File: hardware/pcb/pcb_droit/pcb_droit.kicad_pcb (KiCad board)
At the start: 2 copper layers, 31 x 60 mm, 19 parts, among them P1 TE-FFC-10-0.5

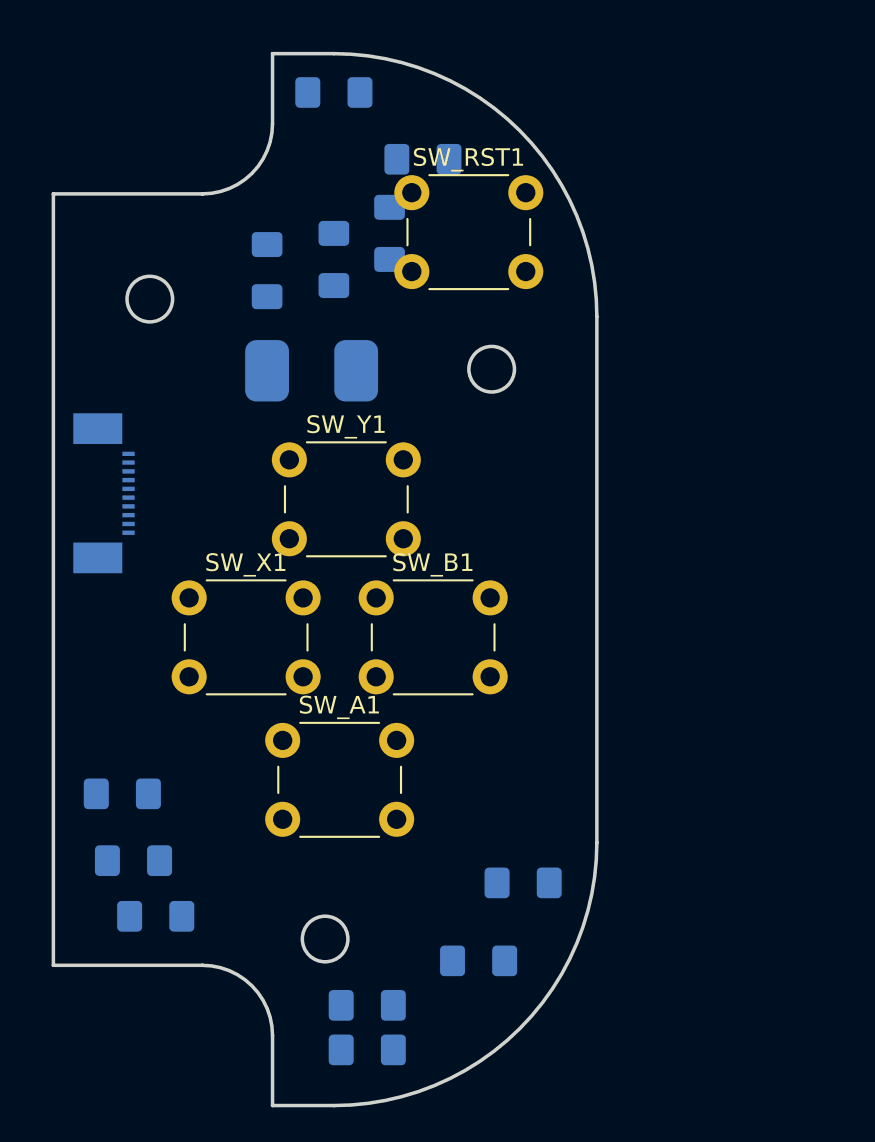
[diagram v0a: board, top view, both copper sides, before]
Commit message: Modifications des fonts et debut de la creation du drivers de touches
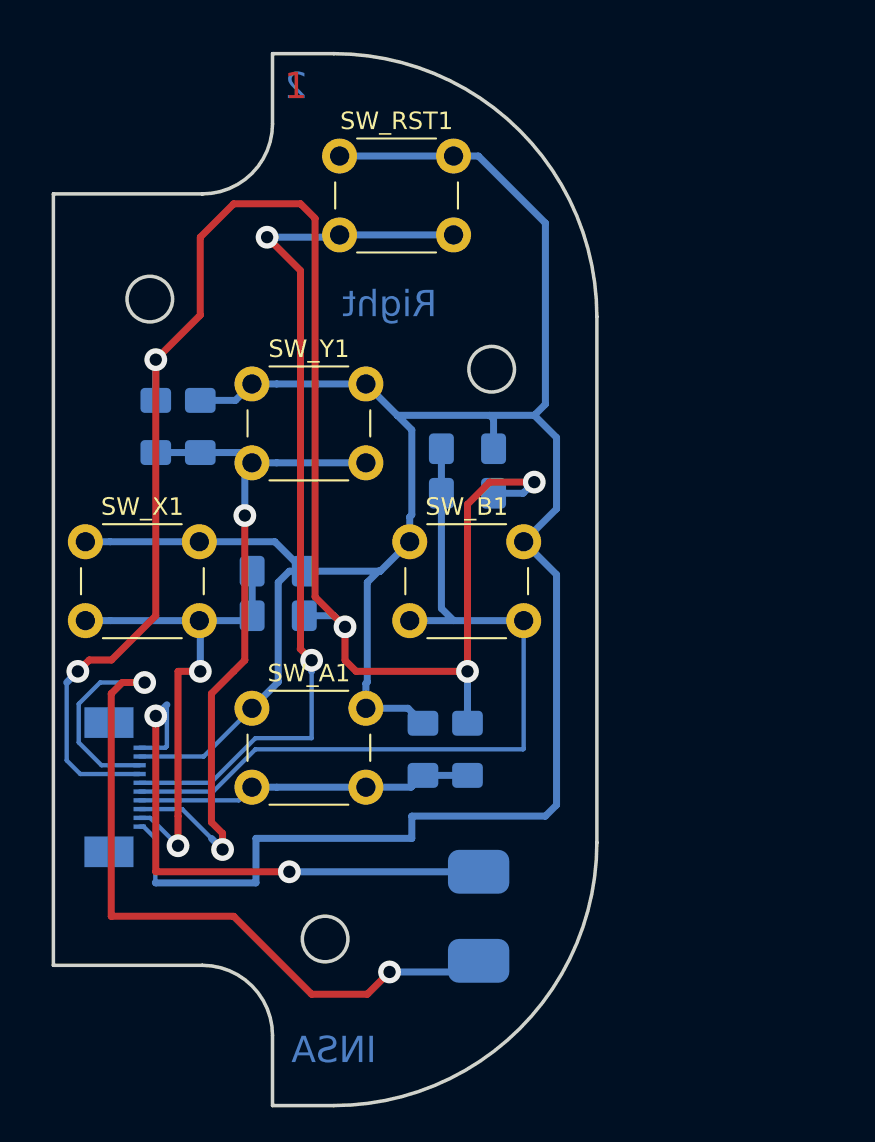
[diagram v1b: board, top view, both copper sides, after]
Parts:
- removed R2, R4, R6, R8: R, Resistor_SMD:R_1206_3216Metric_Pad1.42x1.75mm_HandSolder
- moved C2 34.8 mm to (137.8, 99.7)
- moved LS1 32.5 mm to (138.4, 126.4), turned to 270 degrees
- moved C1 29.5 mm to (135.3, 116.8)
- moved R3 26.1 mm to (137.8, 102.2), turned to 180 degrees
- moved C3 22.6 mm to (127.0, 106.7)
- moved R7 21.6 mm to (120.0, 98.4), turned to 270 degrees
- moved P1 16.8 mm to (118.7, 119.0)
- moved R5 16.2 mm to (127.0, 109.2), turned to 180 degrees
- moved R1 15.7 mm to (137.8, 116.8), turned to 270 degrees
- moved C4 9.67 mm to (122.6, 98.4)
- moved SW_X1 6.73 mm to (116.0, 105.0)
- moved SW_Y1 4.83 mm to (125.5, 96.0)
- moved SW_RST1 4.62 mm to (130.5, 83.0)
- moved SW_B1 3.73 mm to (134.5, 105.0)
- moved SW_A1 2.54 mm to (125.5, 114.5)
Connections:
- C1 pad 1: Net-(C1-Pad1) -> /Key_A
- C2 pad 1: Net-(C2-Pad1) -> /Key_B
- C3 pad 1: Net-(C3-Pad1) -> /Key_X
- C4 pad 1: Net-(C4-Pad1) -> /Key_Y
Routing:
- net GND: track 0.00 -> 158.1 mm
- net VCC: track 0.00 -> 103.4 mm, vias 0 -> 5
- net /Key_Rst: track 0.00 -> 51.2 mm, vias 0 -> 2
- net /Audio_Right_2: track 0.00 -> 48.9 mm, vias 0 -> 2
- net /Key_B: track 0.00 -> 46.8 mm
- net /Key_Y: track 0.00 -> 41.2 mm, vias 0 -> 2
- net /Audio_Right_1: track 0.00 -> 32.2 mm, vias 0 -> 2
- net /Key_X: track 0.00 -> 29.1 mm, vias 0 -> 2
- net /Key_A: track 0.00 -> 19.3 mm
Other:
- board text added: "1"
- board text added: "2"
- board text added: "INSA"
- board text added: "Right"

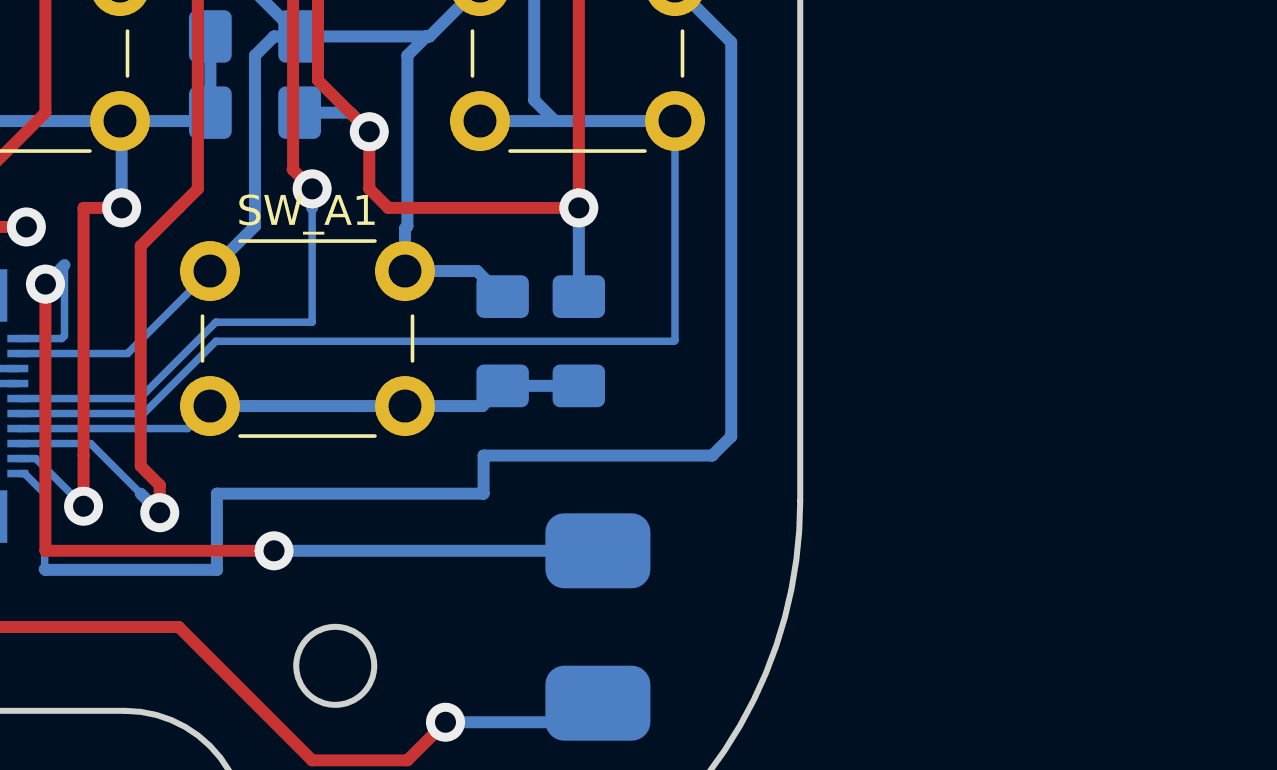
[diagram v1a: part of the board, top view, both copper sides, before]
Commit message: ajout du wifi (debut) et mise a jour pcb
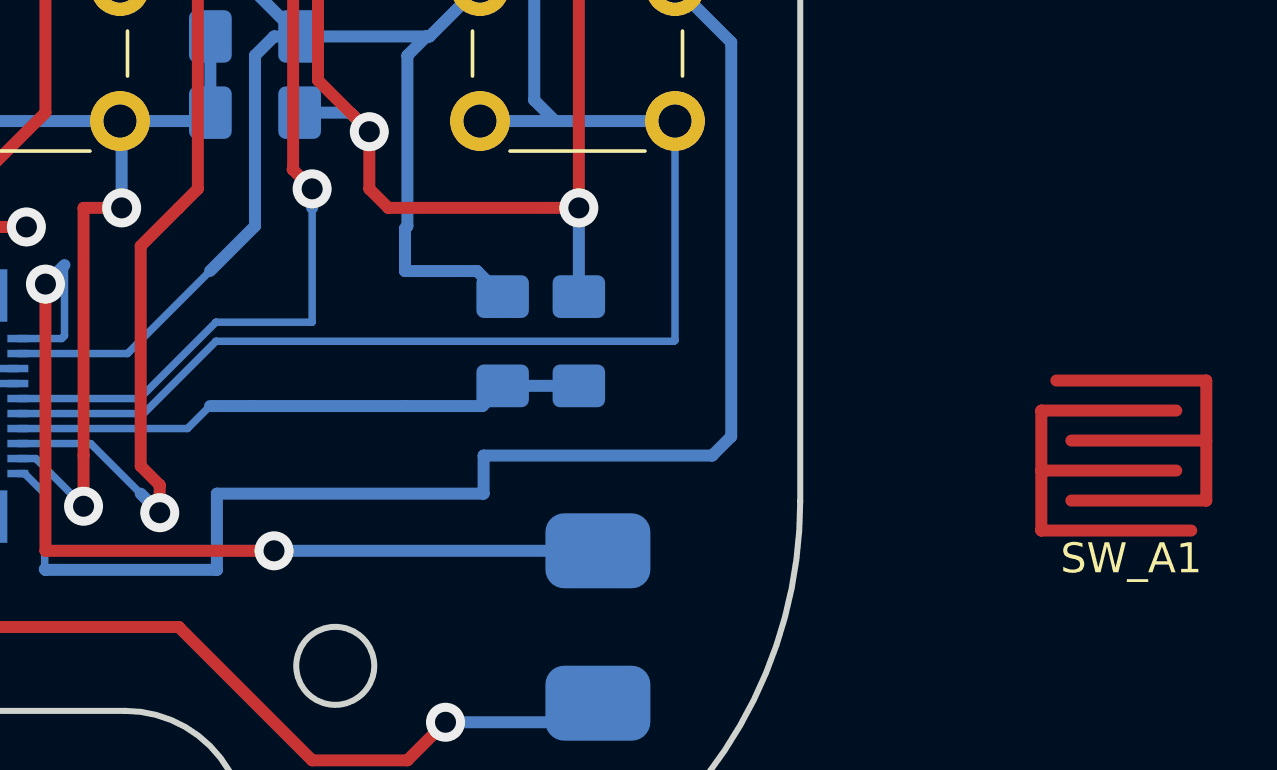
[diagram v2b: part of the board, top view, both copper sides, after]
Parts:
- SW_A1: footprint Button_Switch_THT:SW_PUSH_6mm -> Insa:RubberKey
- moved SW_A1 31.3 mm to (156.2, 120.7)
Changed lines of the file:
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@@
     (add_net VCC)
+  )
+  (module Insa:RubberKey locked (layer F.Cu)
+    (at 156.21 120.65)
+    (fp_text reference SW_A1 (at 0 3.429) (layer F.SilkS)
+      (effects (font (size 1 1) (thickness 0.15)))
+    )
+    (fp_text value SW_Push (at 0.254 -3.937) (layer F.Fab)
+      (effects (font (size 1 1) (thickness 0.15)))
+    )
+    (fp_poly (pts (xy -3.5 -3) (xy 3 -3) (xy 3 3) (xy -3.5 3)) (layer F.Mask) (width 0.15))
+    (pad 2 connect custom (at -3 0 180) (size 0.3 1) (layers F.Cu F.Mask)
+      (net 8 /Key_A) (zone_connect 0)
+      (options (clearance outline) (anchor rect))
+      (primitives
+        (gr_line (start 0 -2.5) (end 0 1.5) (width 0.4))
+        (gr_line (start -5 -2.5) (end 0 -2.5) (width 0.4))
+        (gr_line (start -4.5 1.5) (end 0 1.5) (width 0.4))
+        (gr_line (start -4.5 -0.5) (end 0 -0.5) (width 0.4))
+      ))
+    (pad 1 connect custom (at 2.5 0) (size 0.3 1) (layers F.Cu F.Mask)
+      (net 1 GND) (zone_connect 0)
+      (options (clearance outline) (anchor rect))
+      (primitives
+        (gr_line (start 0 -2.5) (end 0 1.5) (width 0.4))
+        (gr_line (start -5 -2.5) (end 0 -2.5) (width 0.4))
+        (gr_line (start -4.5 1.5) (end 0 1.5) (width 0.4))
+        (gr_line (start -4.5 -0.5) (end 0 -0.5) (width 0.4))
+      ))
   )
   (module Capacitor_SMD:C_1206_3216Metric_Pad1.42x1.75mm_HandSolder (layer B.Cu)
@@
       (at (xyz 0 0 0))
       (scale (xyz 1 1 1))
-      (rotate (xyz 0 0 0))
-    )
-  )
-  (module Button_Switch_THT:SW_PUSH_6mm locked (layer F.Cu)
-    (at 125.5 114.5)
-    (descr https://www.omron.com/ecb/products/pdf/en-b3f.pdf)
-    (tags "tact sw push 6mm")
-    (fp_text reference SW_A1 (at 3.25 -2) (layer F.SilkS)
-      (effects (font (size 1 1) (thickness 0.15)))
-    )
-    (fp_text value SW_Push (at 3.75 6.7) (layer F.Fab)
-      (effects (font (size 1 1) (thickness 0.15)))
-    )
-    (fp_circle (center 3.25 2.25) (end 1.25 2.5) (layer F.Fab) (width 0.1))
-    (fp_line (start 6.75 3) (end 6.75 1.5) (layer F.SilkS) (width 0.12))
-    (fp_line (start 5.5 -1) (end 1 -1) (layer F.SilkS) (width 0.12))
-    (fp_line (start -0.25 1.5) (end -0.25 3) (layer F.SilkS) (width 0.12))
-    (fp_line (start 1 5.5) (end 5.5 5.5) (layer F.SilkS) (width 0.12))
-    (fp_line (start 8 -1.25) (end 8 5.75) (layer F.CrtYd) (width 0.05))
-    (fp_line (start 7.75 6) (end -1.25 6) (layer F.CrtYd) (width 0.05))
-    (fp_line (start -1.5 5.75) (end -1.5 -1.25) (layer F.CrtYd) (width 0.05))
-    (fp_line (start -1.25 -1.5) (end 7.75 -1.5) (layer F.CrtYd) (width 0.05))
-    (fp_line (start -1.5 6) (end -1.25 6) (layer F.CrtYd) (width 0.05))
-    (fp_line (start -1.5 5.75) (end -1.5 6) (layer F.CrtYd) (width 0.05))
-    (fp_line (start -1.5 -1.5) (end -1.25 -1.5) (layer F.CrtYd) (width 0.05))
-    (fp_line (start -1.5 -1.25) (end -1.5 -1.5) (layer F.CrtYd) (width 0.05))
-    (fp_line (start 8 -1.5) (end 8 -1.25) (layer F.CrtYd) (width 0.05))
-    (fp_line (start 7.75 -1.5) (end 8 -1.5) (layer F.CrtYd) (width 0.05))
-    (fp_line (start 8 6) (end 8 5.75) (layer F.CrtYd) (width 0.05))
-    (fp_line (start 7.75 6) (end 8 6) (layer F.CrtYd) (width 0.05))
-    (fp_line (start 0.25 -0.75) (end 3.25 -0.75) (layer F.Fab) (width 0.1))
-    (fp_line (start 0.25 5.25) (end 0.25 -0.75) (layer F.Fab) (width 0.1))
-    (fp_line (start 6.25 5.25) (end 0.25 5.25) (layer F.Fab) (width 0.1))
-    (fp_line (start 6.25 -0.75) (end 6.25 5.25) (layer F.Fab) (width 0.1))
-    (fp_line (start 3.25 -0.75) (end 6.25 -0.75) (layer F.Fab) (width 0.1))
-    (fp_text user %R (at 3.25 2.25) (layer F.Fab)
-      (effects (font (size 1 1) (thickness 0.15)))
-    )
-    (pad 1 thru_hole circle (at 6.5 0 90) (size 2 2) (drill 1.1) (layers *.Cu *.Mask)
-      (net 1 GND))
-    (pad 2 thru_hole circle (at 6.5 4.5 90) (size 2 2) (drill 1.1) (layers *.Cu *.Mask)
-      (net 8 /Key_A))
-    (pad 1 thru_hole circle (at 0 0 90) (size 2 2) (drill 1.1) (layers *.Cu *.Mask)
-      (net 1 GND))
-    (pad 2 thru_hole circle (at 0 4.5 90) (size 2 2) (drill 1.1) (layers *.Cu *.Mask)
-      (net 8 /Key_A))
-    (model ${KISYS3DMOD}/Button_Switch_THT.3dshapes/SW_PUSH_6mm.wrl
-      (at (xyz 0 0 0))
-      (scale (xyz 1 1 1))

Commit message: mise a jour des pcb et design mecaniques
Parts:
- added Logo1: LOGO, Insa:insa-image, F.Cu at (130.8, 101.6)
- added REF**: MountingHole_5mm, MountingHole:MountingHole_5mm, F.Cu at (126.0, 86.5)
- added REF**: MountingHole_5mm, MountingHole:MountingHole_5mm, F.Cu at (128.2, 118.9)
- added REF**: MountingHole_2.7mm_M2.5, MountingHole:MountingHole_2.7mm_M2.5, F.Cu at (138.5, 121.2)
- added REF**: MountingHole_2.7mm_M2.5, MountingHole:MountingHole_2.7mm_M2.5, F.Cu at (120.5, 124.2)
- added REF**: MountingHole_2.7mm_M2.5, MountingHole:MountingHole_2.7mm_M2.5, F.Cu at (130.5, 80.2)
- C1, C2, C3, C4, LS1, P1, R1, R3, R5, R7: moved to F.Cu
- SW_A1: footprint Insa:RubberKey -> Insa:RubberKey-4mm-2; moved to B.Cu
- SW_B1, SW_X1, SW_Y1: footprint Button_Switch_THT:SW_PUSH_6mm -> Insa:RubberKey-4mm-2; moved to B.Cu
- SW_RST1: moved to B.Cu
- moved SW_RST1 51.1 mm to (132.7, 134.1), turned to 90 degrees
- moved SW_A1 38.3 mm to (118.7, 112.7)
- moved R1 19.5 mm to (118.6, 113.1), turned to 180 degrees
- moved LS1 17.8 mm to (128.3, 111.8), turned to 0 degrees
- moved C1 16.7 mm to (118.6, 115.6), turned to 0 degrees
- moved R5 14.8 mm to (120.7, 95.9), turned to 270 degrees
- moved R7 14.3 mm to (134.0, 95.3), turned to 180 degrees
- moved C3 14.0 mm to (118.1, 95.9), turned to 90 degrees
- moved P1 13.5 mm to (118.7, 105.5), turned to 90 degrees
- moved C4 12.7 mm to (134.0, 92.8), turned to 0 degrees
- moved C2 12.2 mm to (138.0, 111.9)
- moved SW_Y1 10.5 mm to (135.5, 92.7)
- moved SW_X1 9.69 mm to (118.7, 95.7)
- moved R3 7.12 mm to (138.0, 109.4)
- moved SW_B1 4.80 mm to (135.5, 109.7)
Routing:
- net GND: track 158.1 -> 120.5 mm, vias 0 -> 6
- net /Audio_Right_2: track 48.9 -> 16.0 mm, vias 2 -> 0
- net /Key_A: track 19.3 -> 44.8 mm, vias 0 -> 4
- net /Audio_Right_1: track 32.2 -> 9.80 mm, vias 2 -> 0
- net /Key_B: track 46.8 -> 25.4 mm, vias 0 -> 1
- net /Key_X: track 29.1 -> 16.9 mm, vias 2 -> 1
- net /Key_Y: track 41.2 -> 30.0 mm, vias 2 -> 1
- net /Key_Rst: track 51.2 -> 42.9 mm, vias 2 -> 0
- net VCC: track 103.4 -> 97.0 mm, vias 5 -> 2
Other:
- board size 31 x 60 mm -> 31 x 59.8 mm
- board text added: "V.02A"
- board text removed: "INSA"
- board text removed: "Right"
